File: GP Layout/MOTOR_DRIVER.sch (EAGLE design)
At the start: 46 parts, among them U3 MIC4604YM, U6 MIC4604YM, U7 ATMEGA328P_TQFP, Y1 16MHz

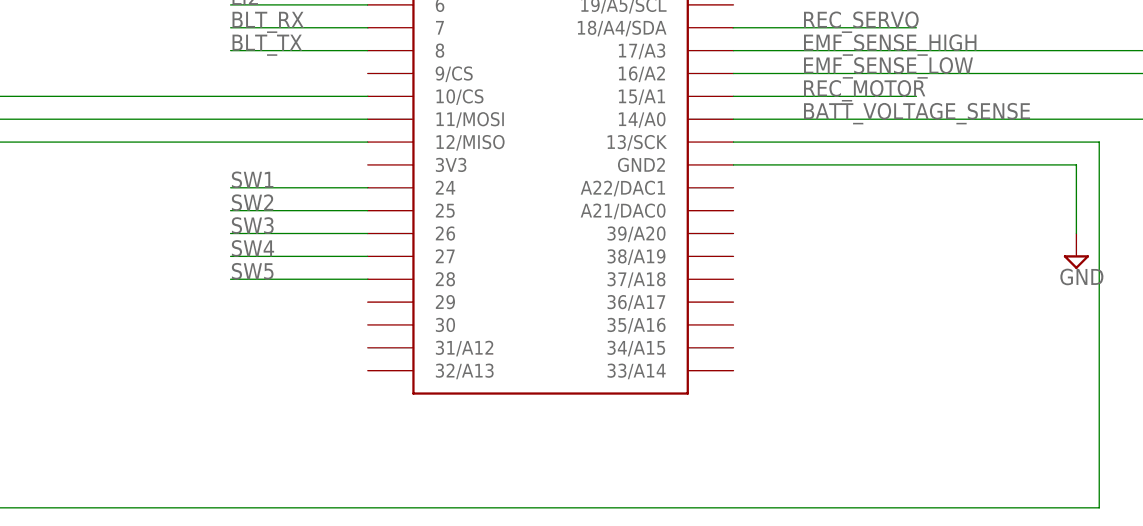
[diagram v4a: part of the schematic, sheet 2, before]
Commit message: added backup pins on Teensy for camera and HES
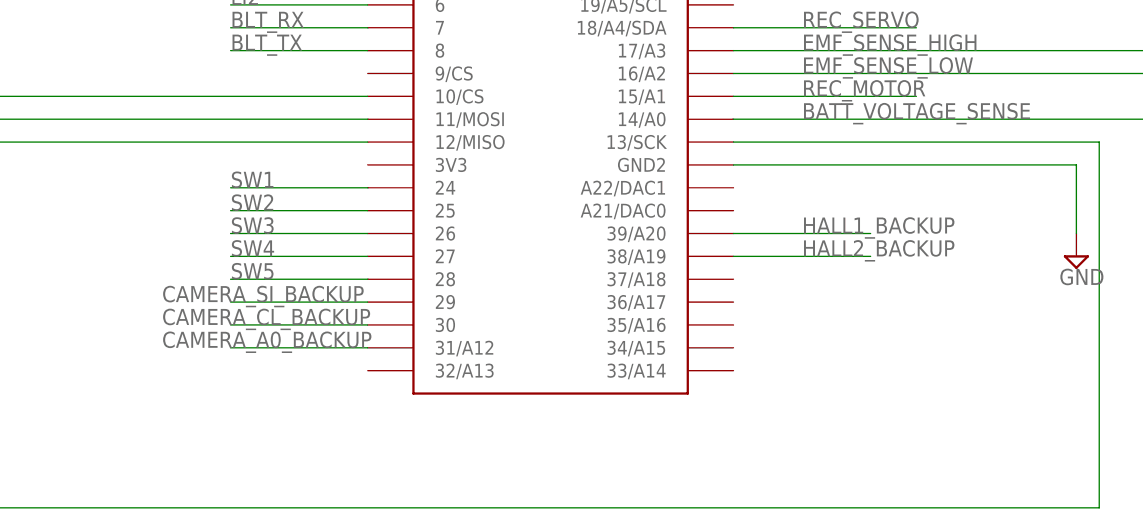
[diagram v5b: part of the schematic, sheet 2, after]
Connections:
- removed net N$36: SV4.7
- removed net N$37: SV4.6
- removed net N$38: SV4.5
- removed net N$39: SV4.4
- removed net N$40: SV4.3
- removed net N$41: SV4.2
- removed net N$42: SV4.1
- new net CAMERA_A0_BACKUP: SV4.1, U$1.31/A12
- new net CAMERA_CL_BACKUP: SV4.2, U$1.30
- new net CAMERA_SI_BACKUP: SV4.3, U$1.29
- new net HALL1_BACKUP: SV4.6, U$1.39/A20
- new net HALL2_BACKUP: SV4.7, U$1.38/A19
- net 3_3V: now also SV4.5
- net GND: now also SV4.4
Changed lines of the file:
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@@
+</segment>
+</net>
+<net name="CAMERA_SI_BACKUP" class="0">
+<segment>
+<pinref part="U$1" gate="G$1" pin="29"/>
+<wire x1="238.76" y1="116.84" x2="223.52" y2="116.84" width="0.1524" layer="91"/>
+<label x="215.9" y="116.84" size="1.778" layer="95"/>
+</segment>
+</net>
+<net name="CAMERA_CL_BACKUP" class="0">
+<segment>
+<pinref part="U$1" gate="G$1" pin="30"/>
+<wire x1="238.76" y1="114.3" x2="223.52" y2="114.3" width="0.1524" layer="91"/>
+<label x="215.9" y="114.3" size="1.778" layer="95"/>
+</segment>
+</net>
+<net name="CAMERA_A0_BACKUP" class="0">
+<segment>
+<pinref part="U$1" gate="G$1" pin="31/A12"/>
+<wire x1="238.76" y1="111.76" x2="223.52" y2="111.76" width="0.1524" layer="91"/>
+<label x="215.9" y="111.76" size="1.778" layer="95"/>
+</segment>
+</net>
+<net name="HALL1_BACKUP" class="0">
+<segment>
+<pinref part="U$1" gate="G$1" pin="39/A20"/>
+<wire x1="279.4" y1="124.46" x2="294.64" y2="124.46" width="0.1524" layer="91"/>
+<label x="287.02" y="124.46" size="1.778" layer="95"/>
+</segment>
+</net>
+<net name="HALL2_BACKUP" class="0">
+<segment>
+<pinref part="U$1" gate="G$1" pin="38/A19"/>
+<wire x1="279.4" y1="121.92" x2="294.64" y2="121.92" width="0.1524" layer="91"/>
+<label x="287.02" y="121.92" size="1.778" layer="95"/>
 </segment>
 </net>
@@
 <label x="302.26" y="149.86" size="1.778" layer="95"/>
 </segment>
+<segment>
+<wire x1="330.2" y1="144.78" x2="353.06" y2="144.78" width="0.1524" layer="91"/>
+<pinref part="SV4" gate="G$1" pin="4"/>
+<label x="340.36" y="144.78" size="1.778" layer="95"/>
+</segment>
 </net>
 <net name="5V" class="0">
@@
 <label x="236.22" y="147.32" size="1.778" layer="95"/>
 </segment>
+<segment>
+<wire x1="330.2" y1="147.32" x2="353.06" y2="147.32" width="0.1524" layer="91"/>
+<pinref part="SV4" gate="G$1" pin="5"/>
+<label x="340.36" y="147.32" size="1.778" layer="95"/>
+</segment>
 </net>
 <net name="CAMERA_CLK" class="0">
@@
 </segment>
 </net>
-<net name="N$36" class="0">
+<net name="HALL2_BACKUP" class="0">
 <segment>
 <wire x1="330.2" y1="152.4" x2="353.06" y2="152.4" width="0.1524" layer="91"/>
 <pinref part="SV4" gate="G$1" pin="7"/>
-</segment>
-</net>
-<net name="N$37" class="0">
+<label x="340.36" y="152.4" size="1.778" layer="95"/>
+</segment>
+</net>
+<net name="HALL1_BACKUP" class="0">
 <segment>
 <wire x1="330.2" y1="149.86" x2="353.06" y2="149.86" width="0.1524" layer="91"/>
 <pinref part="SV4" gate="G$1" pin="6"/>
-</segment>
-</net>
-<net name="N$38" class="0">
-<segment>
-<wire x1="330.2" y1="147.32" x2="353.06" y2="147.32" width="0.1524" layer="91"/>
-<pinref part="SV4" gate="G$1" pin="5"/>
-</segment>
-</net>
-<net name="N$39" class="0">
-<segment>
-<wire x1="330.2" y1="144.78" x2="353.06" y2="144.78" width="0.1524" layer="91"/>
-<pinref part="SV4" gate="G$1" pin="4"/>
-</segment>
-</net>
-<net name="N$40" class="0">
+<label x="340.36" y="149.86" size="1.778" layer="95"/>
+</segment>
+</net>
+<net name="CAMERA_SI_BACKUP" class="0">
 <segment>
 <wire x1="330.2" y1="142.24" x2="353.06" y2="142.24" width="0.1524" layer="91"/>
 <pinref part="SV4" gate="G$1" pin="3"/>
-</segment>
-</net>
-<net name="N$41" class="0">
+<label x="340.36" y="142.24" size="1.778" layer="95"/>
+</segment>
+</net>
+<net name="CAMERA_CL_BACKUP" class="0">
 <segment>
 <wire x1="330.2" y1="139.7" x2="353.06" y2="139.7" width="0.1524" layer="91"/>
 <pinref part="SV4" gate="G$1" pin="2"/>
-</segment>
-</net>
-<net name="N$42" class="0">
+<label x="340.36" y="139.7" size="1.778" layer="95"/>
+</segment>
+</net>
+<net name="CAMERA_A0_BACKUP" class="0">
 <segment>
 <wire x1="330.2" y1="137.16" x2="353.06" y2="137.16" width="0.1524" layer="91"/>
 <pinref part="SV4" gate="G$1" pin="1"/>
-</segment>
-</net>
+<label x="340.36" y="137.16" size="1.778" layer="95"/>
+</segment>
+</net>

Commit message: t :wq # Explicit paths specified without -i or -o; assuming --only paths...
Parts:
- removed D1, D2: BYV32, diode:BYV32
- removed SV3: (no value), con-lsta:FE10-2
- removed SV4: (no value), con-lsta:FE10-1
- removed U$3: LM1086IT-5.0/NOPB, TI1086:LM1086IT-5.0/NOPB
- added BLUETOOTH: (no value), con-lsta:FE04-1
- added CAMERA, CAMERA_B: (no value), con-lsta:FE05-1
- added HALL1, HALL1_B, HALL2, HALL2_B, SERVO: (no value), con-lstb:MA03-1
- added REC: (no value), con-lstb:MA06-1
- added TXRX: (no value), con-lsta:FE02-1
- added VOLT_REG: LM1086TO220V, v-reg-3:LM1086TO220V
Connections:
- removed net CAMERA_A0_BACKUP: SV4.1, U$1.31/A12
- removed net CAMERA_CLK: SV3.13, U7.PB0(ICP)
- removed net CAMERA_CL_BACKUP: SV4.2, U$1.30
- removed net CAMERA_SI_BACKUP: SV4.3, U$1.29
- removed net HALL: SV3.16, U7.PD2(INT0)
- removed net HALL1_BACKUP: SV4.6, U$1.39/A20
- removed net HALL2_BACKUP: SV4.7, U$1.38/A19
- removed net N$1: D1.A1, D1.A2, R3.1, R4.2
- removed net N$20: SV3.4
- removed net N$33: SV4.10
- removed net N$34: SV4.9
- removed net N$35: SV4.8
- new net CAMERA_A0_B: CAMERA_B.3, U$1.31/A12
- new net CAMERA_CL: CAMERA.4, U7.PB0(ICP)
- new net CAMERA_CL_B: CAMERA_B.4, U$1.30
- new net CAMERA_SI_B: CAMERA_B.5, U$1.29
- new net HALL1: HALL1.3, U7.PD2(INT0)
- new net HALL1_B: HALL1_B.3, U$1.39/A20
- new net HALL2: HALL2.3
- new net HALL2_B: HALL2_B.3, U$1.38/A19
- new net REC_EXTRA1: REC.5
- new net REC_EXTRA2: REC.6
- net 3_3V: now also BLUETOOTH.4, CAMERA.2, CAMERA_B.2, HALL1.1, HALL1_B.1, HALL2.1, HALL2_B.1; no longer SV3.9, SV4.5
- net 5V: now also REC.2, SERVO.2, VOLT_REG.OUT; no longer SV1.8, SV3.18, SV3.6, SV3.7, U$3.VOUT
- net 7_4V: now also VOLT_REG.IN; no longer U$3.VIN
- net BLT_RX: now also BLUETOOTH.1; no longer SV3.1
- net BLT_TX: now also BLUETOOTH.2; no longer SV3.3
- net CAMERA_A0: now also CAMERA.3; no longer SV3.17
- net CAMERA_SI: now also CAMERA.5; no longer SV3.15
- net EMF_SENSE_HIGH: now also R3.1, R4.2; no longer D1.C
- net EMF_SENSE_LOW: now also S1.5; no longer D2.C
- net GND: now also BLUETOOTH.3, CAMERA.1, CAMERA_B.1, HALL1.2, HALL1_B.2, HALL2.2, HALL2_B.2, REC.1, SERVO.1, VOLT_REG.GND; no longer S1.8, SV3.11, SV3.12, SV3.14, SV3.2, SV3.5, SV4.4, U$3.ADJ/GND
- net MOTOR_HIGH_TOP: now also SV6.5
- net MOTOR_LOW: now also S1.8; no longer D2.A1, D2.A2
- net MOTOR_LOW_TOP: no longer SV6.5
- net REC_MOTOR: now also REC.3; no longer SV3.8
- net REC_SERVO: now also REC.4; no longer SV3.10
- net RX: now also TXRX.1; no longer SV3.20
- net SERVO: now also SERVO.3; no longer SV1.9
- net SW5: no longer S1.5
- net TX: now also TXRX.2; no longer SV3.19
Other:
- note added: "Bottom left headers (female)"
- note removed: "BLUETOOTH"
- note removed: "Bottom left headers"
- note removed: "Bottom right headers"
- moved on the sheet: C8
